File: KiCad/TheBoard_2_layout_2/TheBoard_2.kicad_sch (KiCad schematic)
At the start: 163 parts, among them J1 Conn_01x03_Female, J2 Conn_01x03_Female, J3 Conn_01x16_Female, J5 Conn_01x16_Female, J6 Conn_01x02_Male, U1 MAX680CSA+T, U10 MCP6074-E/SL, U11 MCP6074-E/SL, U12 MCP6074-E/SL, U13 MCP6074-E/SL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

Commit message: board2-layout2 complete
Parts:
- removed J7: (no value), symbol Connector_Generic:Conn_02x18_Counter_Clockwise
- added J4: DB37_Male_MountingHoles, Connector_Dsub:DSUB-37_Male_Horizontal_P2.77x2.84mm_EdgePinOffset7.70mm_Housed_MountingHolesOffset9.12mm, symbol Connector:DB37_Male_MountingHoles
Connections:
- net at U9.1 (VOUTA), U9.2 (VINA-): now also J4.16
- net at U9.13 (VIND-), U9.14 (VOUTD): now also J4.15
- net at U9.6 (VINB-), U9.7 (VOUTB): now also J4.17
- net at U9.8 (VOUTC), U9.9 (VINC-): now also J4.14
- net at U13.1 (VOUTA), U13.2 (VINA-): now also J4.22
- net at U13.13 (VIND-), U13.14 (VOUTD): now also J4.23
- net at U13.6 (VINB-), U13.7 (VOUTB): now also J4.21
- net at U13.8 (VOUTC), U13.9 (VINC-): now also J4.24
- net at U6.1 (VOUTA), U6.2 (VINA-): now also J4.4
- net at U6.13 (VIND-), U6.14 (VOUTD): now also J4.3
- net at U6.6 (VINB-), U6.7 (VOUTB): now also J4.5
- net at U6.8 (VOUTC), U6.9 (VINC-): now also J4.2
- net at U11.8 (VOUTC), U11.9 (VINC-): now also J4.32
- net at U8.6 (VINB-), U8.7 (VOUTB): now also J4.13
- net at U11.13 (VIND-), U11.14 (VOUTD): now also J4.31
- net at U8.1 (VOUTA), U8.2 (VINA-): now also J4.12
- net at U11.1 (VOUTA), U11.2 (VINA-): now also J4.30
- net at U8.13 (VIND-), U8.14 (VOUTD): now also J4.11
- net at U11.6 (VINB-), U11.7 (VOUTB): now also J4.29
- net at U8.8 (VOUTC), U8.9 (VINC-): now also J4.10
- net at U12.8 (VOUTC), U12.9 (VINC-): now also J4.28
- net at U7.6 (VINB-), U7.7 (VOUTB): now also J4.9
- net at U12.13 (VIND-), U12.14 (VOUTD): now also J4.27
- net at U7.1 (VOUTA), U7.2 (VINA-): now also J4.8
- net at U12.1 (VOUTA), U12.2 (VINA-): now also J4.26
- net at U7.13 (VIND-), U7.14 (VOUTD): now also J4.7
- net at U12.6 (VINB-), U12.7 (VOUTB): now also J4.25
- net at U7.8 (VOUTC), U7.9 (VINC-): now also J4.6
- net at U10.8 (VOUTC), U10.9 (VINC-): now also J4.36
- net at U10.13 (VIND-), U10.14 (VOUTD): now also J4.35
- net at U10.1 (VOUTA), U10.2 (VINA-): now also J4.34
- net at U10.6 (VINB-), U10.7 (VOUTB): now also J4.33
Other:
- moved on the sheet: U6, U8, U9

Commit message: Change pin header to female
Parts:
- J3, J5: footprint Connector_PinHeader_2.54mm:PinHeader_1x16_P2.54mm_Vertical -> (none)
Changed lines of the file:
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@@
     (property "Reference" "J3" (id 0) (at 546.1 163.195 0))
     (property "Value" "Conn_01x16_Female" (id 1) (at 545.465 165.735 0))
-    (property "Footprint" "Connector_PinHeader_2.54mm:PinHeader_1x16_P2.54mm_Vertical" (id 2) (at 549.275 188.595 0)
+    (property "Footprint" "" (id 2) (at 549.275 188.595 0)
       (effects (font (size 1.27 1.27)) hide)
     )
@@
     (property "Reference" "J5" (id 0) (at 22.86 158.75 0))
     (property "Value" "Conn_01x16_Female" (id 1) (at 23.495 161.29 0))
-    (property "Footprint" "Connector_PinHeader_2.54mm:PinHeader_1x16_P2.54mm_Vertical" (id 2) (at 19.685 184.15 0)
+    (property "Footprint" "" (id 2) (at 19.685 184.15 0)
       (effects (font (size 1.27 1.27)) hide)
     )
@@
     )
     (path "/7a4e3353-e1e9-4a1d-9afc-20ec32e9cc1a"
-      (reference "J3") (unit 1) (value "Conn_01x16_Female") (footprint "Connector_PinHeader_2.54mm:PinHeader_1x16_P2.54mm_Vertical")
+      (reference "J3") (unit 1) (value "Conn_01x16_Female") (footprint "Connector_PinSocket_2.54mm:PinSocket_1x16_P2.54mm_Vertical")
     )
     (path "/1263773d-8ba4-4c43-acb3-5193e0fa6b05"
@@
     )
     (path "/8e6013b4-e104-46a8-b12e-cbcbf0a129da"
-      (reference "J5") (unit 1) (value "Conn_01x16_Female") (footprint "Connector_PinHeader_2.54mm:PinHeader_1x16_P2.54mm_Vertical")
+      (reference "J5") (unit 1) (value "Conn_01x16_Female") (footprint "Connector_PinSocket_2.54mm:PinSocket_1x16_P2.54mm_Vertical")
     )
     (path "/df29c39d-03bb-4a8d-885a-396fd4de1466"

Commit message: Adding jumpers, checking GND
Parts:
- added J7: Conn_01x02_Pin, Connector_PinHeader_2.54mm:PinHeader_1x02_P2.54mm_Vertical, symbol Connector:Conn_01x02_Pin
- added J8: Conn_01x02_Male, Connector_PinHeader_2.54mm:PinHeader_1x02_P2.54mm_Vertical, symbol Connector:Conn_01x02_Male
- J3, J5: footprint (none) -> Connector_PinSocket_2.54mm:PinSocket_1x16_P2.54mm_Vertical
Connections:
- net +5V: now also J8.2 (Pin_2); no longer U1.6 (VCC)
- net -5V: now also J7.2 (Pin_2); no longer C5.2, R2.2, U2.3 (VO)
- new net: J8.1 (Pin_1), U1.6 (VCC)
- new net: C5.2, J7.1 (Pin_1), R2.2, U2.3 (VO)

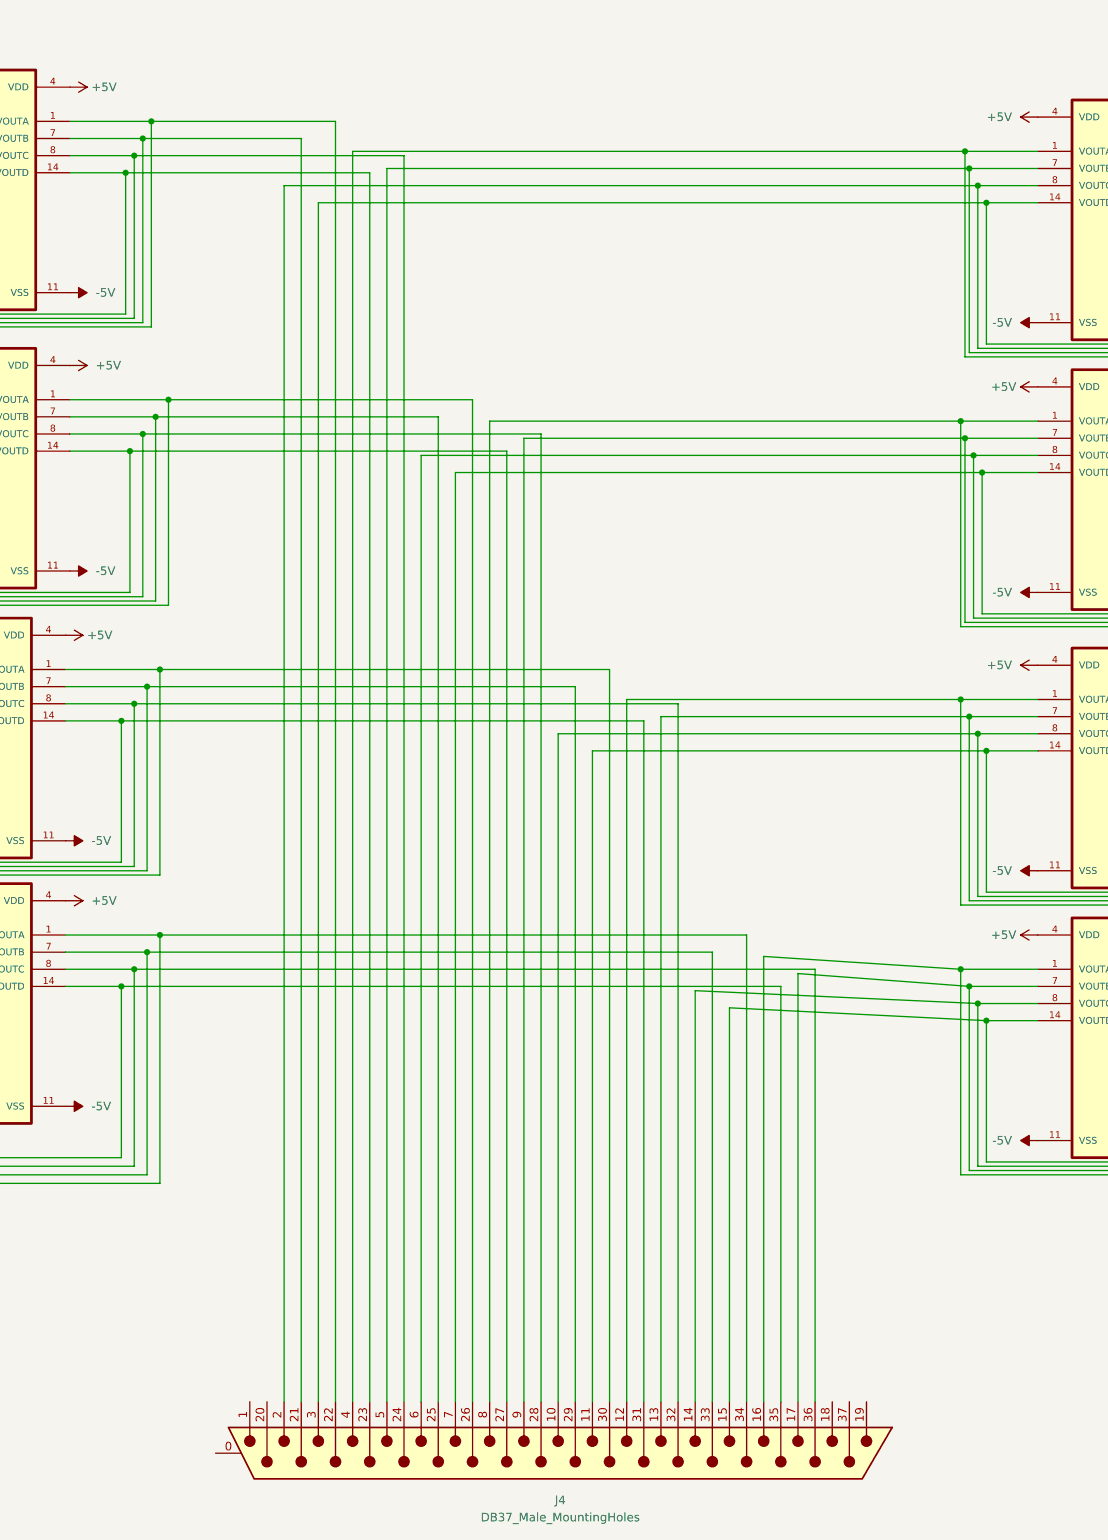
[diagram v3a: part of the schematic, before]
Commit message: Re-routing power
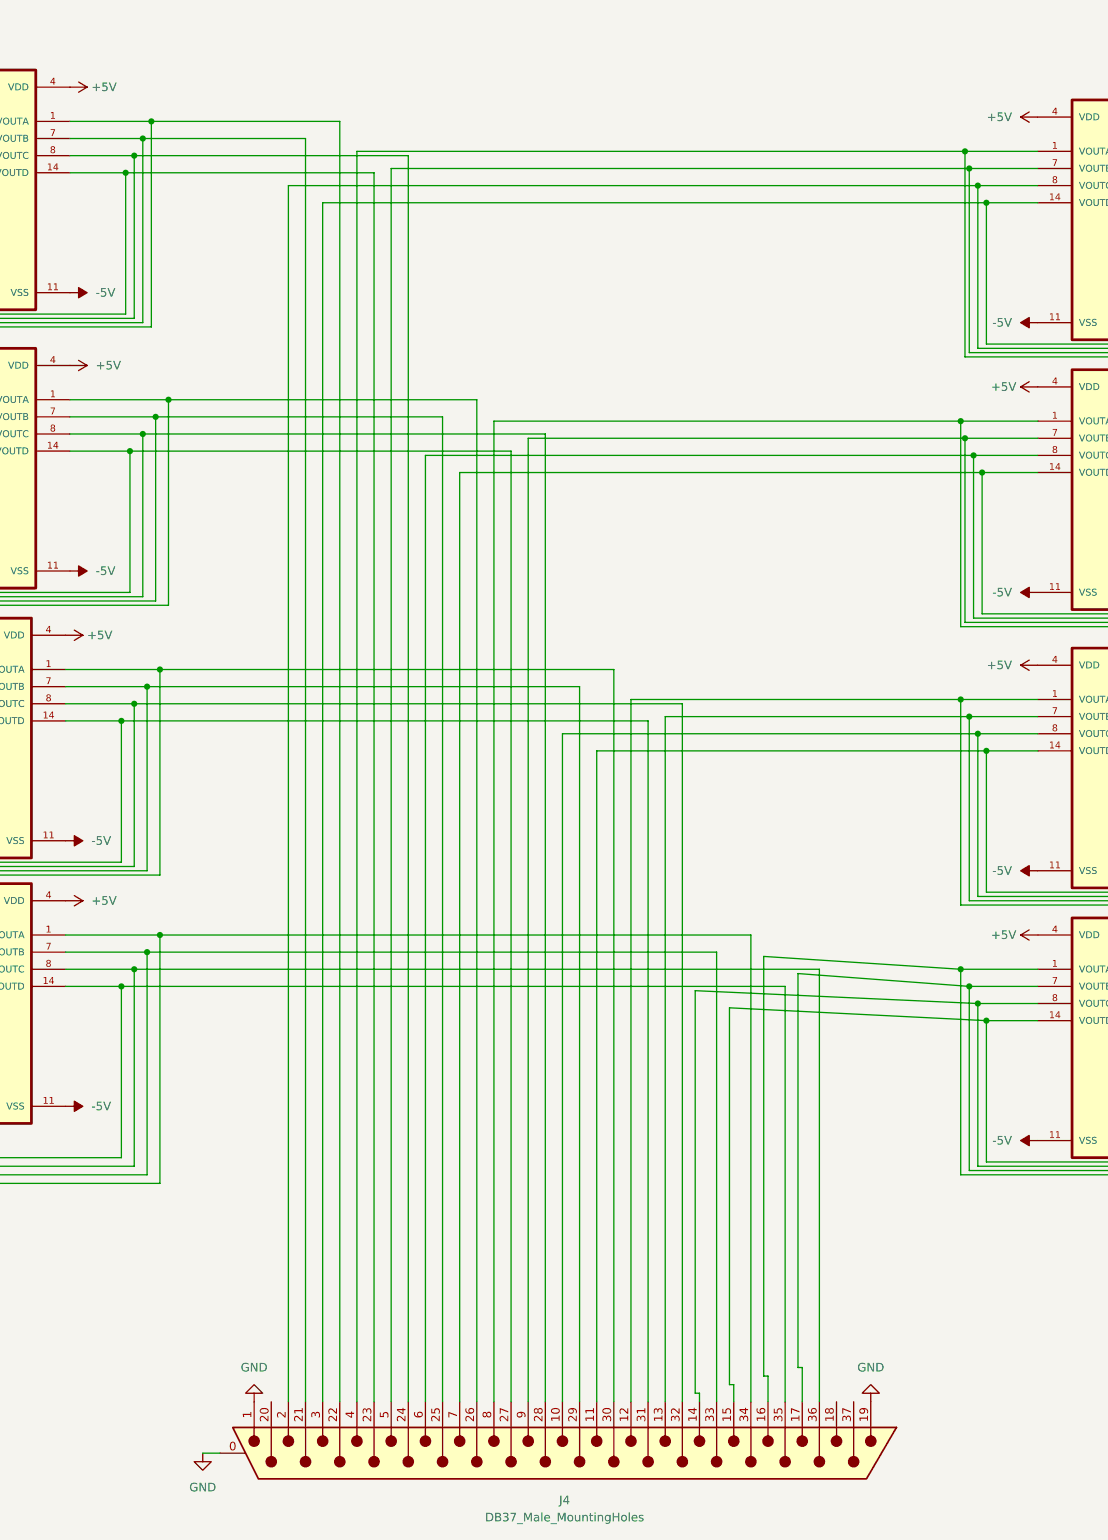
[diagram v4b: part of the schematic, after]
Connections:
- net GND: now also J4.0 (PAD), J4.1, J4.19
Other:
- moved on the sheet: J4

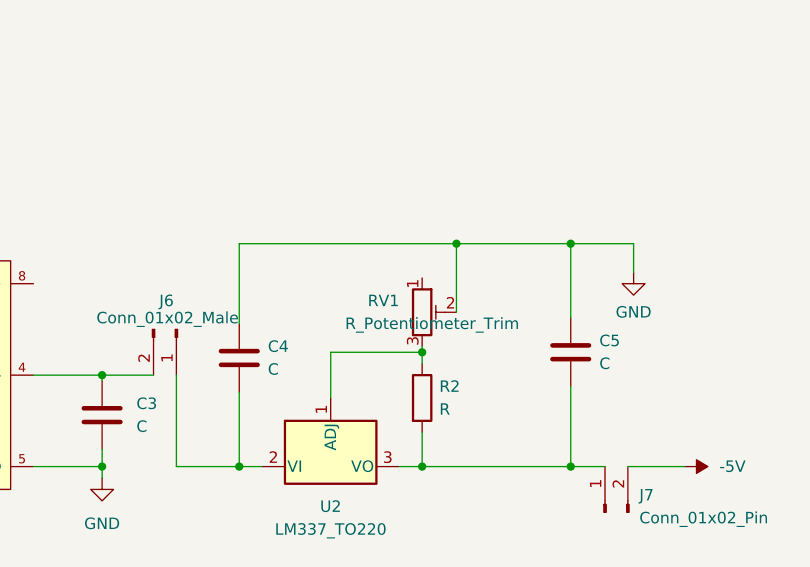
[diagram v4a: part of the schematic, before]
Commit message: Adding gnd to pot, cleaning vias and tracks
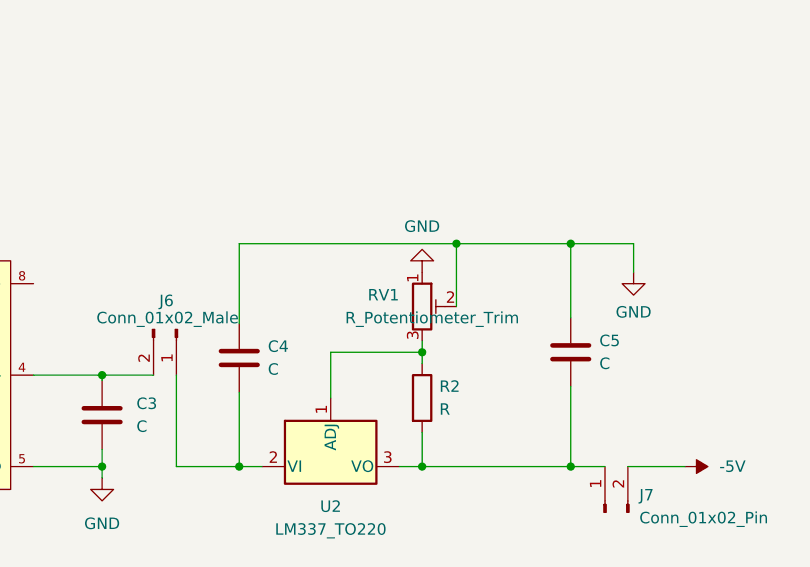
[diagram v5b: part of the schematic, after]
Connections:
- net GND: now also RV1.1
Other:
- moved on the sheet: RV1
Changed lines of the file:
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@@
     (stroke (width 0) (type default))
   )
-  (wire (pts (xy 332.74 56.515) (xy 332.74 57.15))
-    (stroke (width 0) (type default))
-  )
   (wire (pts (xy 28.575 123.19) (xy 28.575 171.45))
     (stroke (width 0) (type default))
@@
     (stroke (width 0) (type default))
   )
+  (wire (pts (xy 332.74 55.88) (xy 332.74 57.15))
+    (stroke (width 0) (type default))
+  )
   (wire (pts (xy 466.09 182.245) (xy 474.98 182.245))
     (stroke (width 0) (type default))
@@
     (stroke (width 0) (type default))
   )
-  (wire (pts (xy 336.55 45.085) (xy 336.55 52.705))
+  (wire (pts (xy 336.55 45.085) (xy 336.55 52.07))
     (stroke (width 0) (type default))
   )
@@
     )
   )
-  (symbol (lib_id "Device:R_Potentiometer_Trim") (at 332.74 52.705 0) (unit 1)
+  (symbol (lib_id "Device:R_Potentiometer_Trim") (at 332.74 52.07 0) (unit 1)
     (in_bom yes) (on_board yes) (dnp no)
-    (property "Reference" "RV1" (at 330.2 51.4349 0)
+    (property "Reference" "RV1" (at 330.2 50.7999 0)
       (effects (font (size 1.27 1.27)) (justify right))
     )
-    (property "Value" "R_Potentiometer_Trim" (at 343.535 53.975 0)
+    (property "Value" "R_Potentiometer_Trim" (at 343.535 53.34 0)
       (effects (font (size 1.27 1.27)) (justify right))
     )
-    (property "Footprint" "Potentiometer_THT:Potentiometer_Bourns_3296W_Vertical" (at 332.74 52.705 0)
+    (property "Footprint" "Potentiometer_THT:Potentiometer_Bourns_3296W_Vertical" (at 332.74 52.07 0)
       (effects (font (size 1.27 1.27)) hide)
     )
-    (property "Datasheet" "~" (at 332.74 52.705 0)
+    (property "Datasheet" "~" (at 332.74 52.07 0)
       (effects (font (size 1.27 1.27)) hide)
     )
@@
         )
       )
+    )
+  )
+  (symbol (lib_name "GND_2") (lib_id "power:GND") (at 332.74 48.26 180) (unit 1)
+    (in_bom yes) (on_board yes) (dnp no) (fields_autoplaced)
+    (property "Reference" "#PWR04" (at 332.74 41.91 0)
+      (effects (font (size 1.27 1.27)) hide)
+    )
+    (property "Value" "GND" (at 332.74 43.18 0)
+      (effects (font (size 1.27 1.27)))
+    )
+    (property "Footprint" "" (at 332.74 48.26 0)
+      (effects (font (size 1.27 1.27)) hide)
+    )
+    (property "Datasheet" "" (at 332.74 48.26 0)
+      (effects (font (size 1.27 1.27)) hide)
+    )
+    (pin "1")
+    (instances
+      (project "TheBoard_2"
+        (path "/0c778962-202e-4f17-a8d9-b9eec2aa2bb0"
+          (reference "#PWR04") (unit 1)
+        )
+      )
